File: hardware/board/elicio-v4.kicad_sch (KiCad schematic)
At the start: 67 parts, among them J2 202656-0021, J3 HDR-3-RA, J4 TC2030-NL, P1 SIG1, P2 SIG2, P3 REF, P4 CHARGE_VBUS, P5 CHARGE_GND, Q1 WPM3027-3, Q2 PMZ290UNE2, Q3 PMZ290UNE2, Q4 PMZ290UNE2, SW1 1TS015A, U1 ISP1807-LR, U2 ADS1292IRSMT, U3 BQ25100YFPR, U4 TLV71330PDQNT, U5 TPS7A0230PDQNR

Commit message: board(v4): add bias-rated charger bypasses and reroute release
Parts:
- added C18, C19: 10uF, Capacitor_SMD:C_0402_1005Metric, symbol Device:C
- C14: value 4.7uF -> 10uF; LCSC (none) -> CONSIGNED; MPN (none) -> GRM155R61A106ME18
- C3: value 1uF -> 10uF; footprint Capacitor_SMD:C_0201_0603Metric -> Capacitor_SMD:C_0402_1005Metric; LCSC C5142566 -> CONSIGNED; MPN TCC0201X5R105K6R3ZT -> GRM155R61A106ME18
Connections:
- net GND: now also C18.2, C19.2
- net TS: now also C18.1
- net VBAT: now also C19.1

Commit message: Mark unverified and unavailable v4 part supply as consigned
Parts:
- C2: LCSC C43380 -> CONSIGNED
- D1: LCSC C24109 -> CONSIGNED
- D2: LCSC C72043 -> CONSIGNED
- R11: LCSC C4104700 -> CONSIGNED
- R18, R19: LCSC (none) -> CONSIGNED
- U3: LCSC C527572 -> CONSIGNED
- U4: LCSC C3071062 -> CONSIGNED
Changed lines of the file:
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@@
 			)
 		)
-		(property "LCSC" "C527572"
+		(property "LCSC" "CONSIGNED"
 			(at 236.22 43.18 0)
 			(show_name no)
@@
 			)
 		)
-		(property "LCSC" "C3071062"
+		(property "LCSC" "CONSIGNED"
 			(at 307.34 40.64 0)
 			(show_name no)
@@
 			)
 		)
-		(property "LCSC" "C24109"
+		(property "LCSC" "CONSIGNED"
 			(at 157.48 185.42 0)
 			(show_name no)
@@
 			)
 		)
-		(property "LCSC" "C72043"
+		(property "LCSC" "CONSIGNED"
 			(at 210.82 185.42 0)
 			(show_name no)
@@
 			)
 		)
-		(property "LCSC" "C4104700"
+		(property "LCSC" "CONSIGNED"
 			(at 185.42 259.08 0)
 			(show_name no)
@@
 			)
 		)
-		(property "LCSC" ""
+		(property "LCSC" "CONSIGNED"
 			(at 505.46 259.08 0)
 			(show_name no)
@@
 			)
 		)
-		(property "LCSC" ""
+		(property "LCSC" "CONSIGNED"
 			(at 48.26 289.56 0)
 			(show_name no)
@@
 			)
 		)
-		(property "LCSC" "C43380"
+		(property "LCSC" "CONSIGNED"
 			(at 93.98 322.58 0)
 			(show_name no)

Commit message: Qualify stocked v4 board parts and document three consignments
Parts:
- C14, C18, C19, C3: LCSC CONSIGNED -> C36626211; MPN GRM155R61A106ME18 -> GRM155R61A106ME18D
- C2: LCSC CONSIGNED -> C5142551; MPN 0201B103K500NT -> TCC0201X7R103K500ZT
- D1: LCSC CONSIGNED -> C3001948
- D2: LCSC CONSIGNED -> C364549; MPN 19-217/GHC-YR1S2/3T -> LTST-C281TGKT-5A
- R11: LCSC CONSIGNED -> C423451; MPN ERJ-1GNF6801C -> 0201WMF6801TEE
- R18: LCSC CONSIGNED -> C270345
- R19: LCSC CONSIGNED -> C270351
- U4: LCSC CONSIGNED -> C2863576; MPN TLV71330PDQNT -> TLV71330PDQNR
- U5: LCSC CONSIGNED -> C2867950
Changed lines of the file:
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@@
 			)
 		)
-		(property "LCSC" "CONSIGNED"
+		(property "LCSC" "C2863576"
 			(at 307.34 40.64 0)
 			(show_name no)
@@
 			)
 		)
-		(property "MPN" "TLV71330PDQNT"
+		(property "MPN" "TLV71330PDQNR"
 			(at 307.34 40.64 0)
 			(show_name no)
@@
 			)
 		)
-		(property "LCSC" "CONSIGNED"
+		(property "LCSC" "C2867950"
 			(at 383.54 40.64 0)
 			(show_name no)
@@
 			)
 		)
-		(property "LCSC" "CONSIGNED"
+		(property "LCSC" "C3001948"
 			(at 157.48 185.42 0)
 			(show_name no)
@@
 			)
 		)
-		(property "LCSC" "CONSIGNED"
+		(property "LCSC" "C364549"
 			(at 210.82 185.42 0)
 			(show_name no)
@@
 			)
 		)
-		(property "MPN" "19-217/GHC-YR1S2/3T"
+		(property "MPN" "LTST-C281TGKT-5A"
 			(at 210.82 185.42 0)
 			(show_name no)
@@
 			)
 		)
-		(property "LCSC" "CONSIGNED"
+		(property "LCSC" "C423451"
 			(at 185.42 259.08 0)
 			(show_name no)
@@
 			)
 		)
-		(property "MPN" "ERJ-1GNF6801C"
+		(property "MPN" "0201WMF6801TEE"
 			(at 185.42 259.08 0)
 			(show_name no)
@@
 			)
 		)
-		(property "LCSC" "CONSIGNED"
+		(property "LCSC" "C270345"
 			(at 505.46 259.08 0)
 			(show_name no)
@@
 			)
 		)
-		(property "LCSC" "CONSIGNED"
+		(property "LCSC" "C270351"
 			(at 48.26 289.56 0)
 			(show_name no)
@@
 			)
 		)
-		(property "LCSC" "CONSIGNED"
+		(property "LCSC" "C5142551"
 			(at 93.98 322.58 0)
 			(show_name no)
@@
 			)
 		)
-		(property "MPN" "0201B103K500NT"
+		(property "MPN" "TCC0201X7R103K500ZT"
 			(at 93.98 322.58 0)
 			(show_name no)
@@
 			)
 		)
-		(property "LCSC" "CONSIGNED"
+		(property "LCSC" "C36626211"
 			(at 139.70 322.58 0)
 			(show_name no)
@@
 			)
 		)
-		(property "MPN" "GRM155R61A106ME18"
+		(property "MPN" "GRM155R61A106ME18D"
 			(at 139.70 322.58 0)
 			(show_name no)
@@
 			)
 		)
-		(property "LCSC" "CONSIGNED"
+		(property "LCSC" "C36626211"
 			(at 139.70 355.60 0)
 			(show_name no)
@@
 			)
 		)
-		(property "MPN" "GRM155R61A106ME18"
+		(property "MPN" "GRM155R61A106ME18D"
 			(at 139.70 355.60 0)
 			(show_name no)
@@
 			)
 		)
-		(property "LCSC" "CONSIGNED"
+		(property "LCSC" "C36626211"
 			(at 185.42 355.60 0)
 			(show_name no)
@@
 			)
 		)
-		(property "MPN" "GRM155R61A106ME18"
+		(property "MPN" "GRM155R61A106ME18D"
 			(at 185.42 355.60 0)
 			(show_name no)
@@
 			)
 		)
-		(property "LCSC" "CONSIGNED"
+		(property "LCSC" "C36626211"
 			(at 231.14 355.60 0)
 			(show_name no)
@@
 			)
 		)
-		(property "MPN" "GRM155R61A106ME18"
+		(property "MPN" "GRM155R61A106ME18D"
 			(at 231.14 355.60 0)
 			(show_name no)

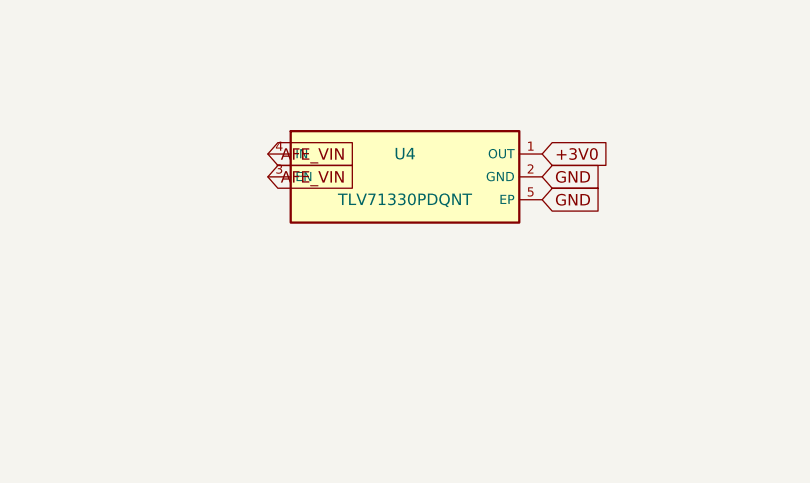
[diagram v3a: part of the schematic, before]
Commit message: review(fab): align regulator value with stocked part and flag stale cost ranges
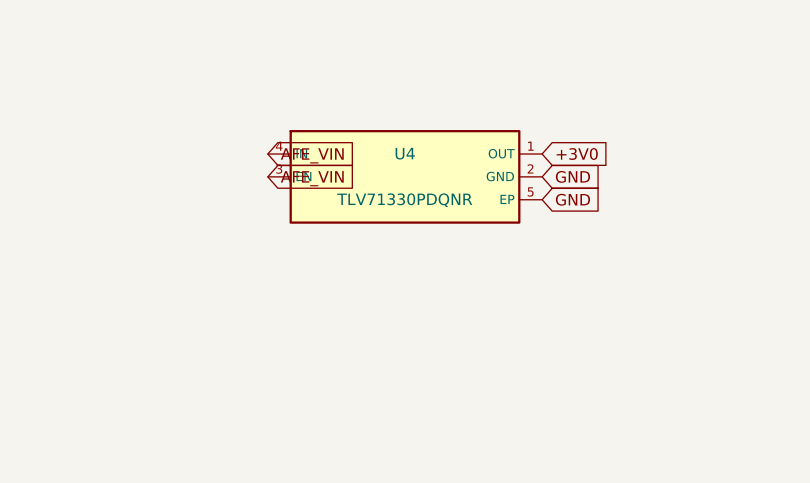
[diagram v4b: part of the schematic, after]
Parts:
- U4: value TLV71330PDQNT -> TLV71330PDQNR
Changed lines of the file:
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@@
 			)
 		)
-		(property "Value" "TLV71330PDQNT"
+		(property "Value" "TLV71330PDQNR"
 			(at 307.34 43.18 0)
 			(show_name no)
